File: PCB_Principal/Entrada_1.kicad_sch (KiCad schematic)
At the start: 17 parts, among them U21 TL071

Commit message: Iniciando PCB...
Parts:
- U101: renamed from U21; footprint Package_DIP:CERDIP-8_W7.62mm_SideBrazed_LongPads_Socket -> Package_DIP:CERDIP-8_W7.62mm_SideBrazed_LongPads
- renumbered C21 to C101, C22 to C102, C23 to C103, C24 to C104, C25 to C105, D21 to D101, D22 to D102, R21 to R101, R22 to R102, R23 to R103, R24 to R104, R25 to R105, R26 to R106, R27 to R107, R28 to R108, RV21 to RV101
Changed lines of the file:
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@@
 		(on_board yes)
 		(dnp no)
-		(property "Reference" "R21"
+		(property "Reference" "R101"
 			(at 91.44 89.408 90)
 			(effects
@@
 			(project "ISPEL-CAD_v1"
 				(path "/f66f0001-c0b9-4d2c-a26f-f2bac9dfd594/c2e6e06f-39d1-4f26-9e70-a3bc9c97e1f0"
-					(reference "R21")
+					(reference "R101")
 					(unit 1)
 				)
@@
 		(on_board yes)
 		(dnp no)
-		(property "Reference" "RV21"
+		(property "Reference" "RV101"
 			(at 143.51 106.68 90)
 			(effects
@@
 			(project "ISPEL-CAD_v1"
 				(path "/f66f0001-c0b9-4d2c-a26f-f2bac9dfd594/c2e6e06f-39d1-4f26-9e70-a3bc9c97e1f0"
-					(reference "RV21")
+					(reference "RV101")
 					(unit 1)
 				)
@@
 		(dnp no)
 		(fields_autoplaced yes)
-		(property "Reference" "#PWR027"
+		(property "Reference" "#PWR0107"
 			(at 208.28 113.03 0)
 			(effects
@@
 			(project "ISPEL-CAD_v1"
 				(path "/f66f0001-c0b9-4d2c-a26f-f2bac9dfd594/c2e6e06f-39d1-4f26-9e70-a3bc9c97e1f0"
-					(reference "#PWR027")
+					(reference "#PWR0107")
 					(unit 1)
 				)
@@
 		(on_board yes)
 		(dnp no)
-		(property "Reference" "R28"
+		(property "Reference" "R108"
 			(at 209.55 100.33 0)
 			(effects
@@
 			(project "ISPEL-CAD_v1"
 				(path "/f66f0001-c0b9-4d2c-a26f-f2bac9dfd594/c2e6e06f-39d1-4f26-9e70-a3bc9c97e1f0"
-					(reference "R28")
+					(reference "R108")
 					(unit 1)
 				)
@@
 		(dnp no)
 		(fields_autoplaced yes)
-		(property "Reference" "D22"
+		(property "Reference" "D102"
 			(at 100.33 109.2199 90)
 			(effects
@@
 			(project "ISPEL-CAD_v1"
 				(path "/f66f0001-c0b9-4d2c-a26f-f2bac9dfd594/c2e6e06f-39d1-4f26-9e70-a3bc9c97e1f0"
-					(reference "D22")
+					(reference "D102")
 					(unit 1)
 				)
@@
 		(dnp no)
 		(fields_autoplaced yes)
-		(property "Reference" "D21"
+		(property "Reference" "D101"
 			(at 100.33 71.1199 90)
 			(effects
@@
 			(project ""
 				(path "/f66f0001-c0b9-4d2c-a26f-f2bac9dfd594/c2e6e06f-39d1-4f26-9e70-a3bc9c97e1f0"
-					(reference "D21")
+					(reference "D101")
 					(unit 1)
 				)
@@
 		(dnp no)
 		(fields_autoplaced yes)
-		(property "Reference" "C25"
+		(property "Reference" "C105"
 			(at 217.17 73.66 90)
 			(effects
@@
 			(project "ISPEL-CAD_v1"
 				(path "/f66f0001-c0b9-4d2c-a26f-f2bac9dfd594/c2e6e06f-39d1-4f26-9e70-a3bc9c97e1f0"
-					(reference "C25")
+					(reference "C105")
 					(unit 1)
 				)
@@
 		(on_board yes)
 		(dnp no)
-		(property "Reference" "C24"
+		(property "Reference" "C104"
 			(at 146.05 125.222 90)
 			(effects
@@
 			(project "ISPEL-CAD_v1"
 				(path "/f66f0001-c0b9-4d2c-a26f-f2bac9dfd594/c2e6e06f-39d1-4f26-9e70-a3bc9c97e1f0"
-					(reference "C24")
+					(reference "C104")
 					(unit 1)
 				)
@@
 		(on_board yes)
 		(dnp no)
-		(property "Reference" "R25"
+		(property "Reference" "R105"
 			(at 195.58 86.36 0)
 			(effects
@@
 			(project "ISPEL-CAD_v1"
 				(path "/f66f0001-c0b9-4d2c-a26f-f2bac9dfd594/c2e6e06f-39d1-4f26-9e70-a3bc9c97e1f0"
-					(reference "R25")
+					(reference "R105")
 					(unit 1)
 				)
@@
 		(on_board yes)
 		(dnp no)
-		(property "Reference" "R22"
+		(property "Reference" "R102"
 			(at 104.14 89.408 90)
 			(effects
@@
 			(project "ISPEL-CAD_v1"
 				(path "/f66f0001-c0b9-4d2c-a26f-f2bac9dfd594/c2e6e06f-39d1-4f26-9e70-a3bc9c97e1f0"
-					(reference "R22")
+					(reference "R102")
 					(unit 1)
 				)
@@
 		(dnp no)
 		(fields_autoplaced yes)
-		(property "Reference" "#PWR026"
+		(property "Reference" "#PWR0105"
 			(at 152.4 127 0)
 			(effects
@@
 			(project "ISPEL-CAD_v1"
 				(path "/f66f0001-c0b9-4d2c-a26f-f2bac9dfd594/c2e6e06f-39d1-4f26-9e70-a3bc9c97e1f0"
-					(reference "#PWR026")
+					(reference "#PWR0105")
 					(unit 1)
 				)
@@
 		(dnp no)
 		(fields_autoplaced yes)
-		(property "Reference" "#PWR028"
+		(property "Reference" "#PWR0108"
 			(at 222.25 90.17 0)
 			(effects
@@
 			(project "ISPEL-CAD_v1"
 				(path "/f66f0001-c0b9-4d2c-a26f-f2bac9dfd594/c2e6e06f-39d1-4f26-9e70-a3bc9c97e1f0"
-					(reference "#PWR028")
+					(reference "#PWR0108")
 					(unit 1)
 				)
@@
 		(dnp no)
 		(fields_autoplaced yes)
-		(property "Reference" "#PWR025"
+		(property "Reference" "#PWR0104"
 			(at 152.4 76.2 0)
 			(effects
@@
 			(project "ISPEL-CAD_v1"
 				(path "/f66f0001-c0b9-4d2c-a26f-f2bac9dfd594/c2e6e06f-39d1-4f26-9e70-a3bc9c97e1f0"
-					(reference "#PWR025")
+					(reference "#PWR0104")
 					(unit 1)
 				)
@@
 		(dnp no)
 		(fields_autoplaced yes)
-		(property "Reference" "C21"
+		(property "Reference" "C101"
 			(at 87.63 96.5262 0)
 			(effects
@@
 			(project "ISPEL-CAD_v1"
 				(path "/f66f0001-c0b9-4d2c-a26f-f2bac9dfd594/c2e6e06f-39d1-4f26-9e70-a3bc9c97e1f0"
-					(reference "C21")
+					(reference "C101")
 					(unit 1)
 				)
@@
 		(on_board yes)
 		(dnp no)
-		(property "Reference" "R24"
+		(property "Reference" "R104"
 			(at 185.42 91.948 90)
 			(effects
@@
 			(project "ISPEL-CAD_v1"
 				(path "/f66f0001-c0b9-4d2c-a26f-f2bac9dfd594/c2e6e06f-39d1-4f26-9e70-a3bc9c97e1f0"
-					(reference "R24")
+					(reference "R104")
 					(unit 1)
 				)
@@
 		(on_board yes)
 		(dnp no)
-		(property "Reference" "U21"
+		(property "Reference" "U101"
 			(at 142.24 86.36 0)
 			(effects
@@
 			)
 		)
-		(property "Footprint" "Package_DIP:CERDIP-8_W7.62mm_SideBrazed_LongPads_Socket"
+		(property "Footprint" "Package_DIP:CERDIP-8_W7.62mm_SideBrazed_LongPads"
 			(at 140.97 92.71 0)
 			(effects
@@
 			(project "ISPEL-CAD_v1"
 				(path "/f66f0001-c0b9-4d2c-a26f-f2bac9dfd594/c2e6e06f-39d1-4f26-9e70-a3bc9c97e1f0"
-					(reference "U21")
+					(reference "U101")
 					(unit 1)
 				)
@@
 		(on_board yes)
 		(dnp no)
-		(property "Reference" "R27"
+		(property "Reference" "R107"
 			(at 209.55 86.36 0)
 			(effects
@@
 			(project "ISPEL-CAD_v1"
 				(path "/f66f0001-c0b9-4d2c-a26f-f2bac9dfd594/c2e6e06f-39d1-4f26-9e70-a3bc9c97e1f0"
-					(reference "R27")
+					(reference "R107")
 					(unit 1)
 				)
@@
 		(dnp no)
 		(fields_autoplaced yes)
-		(property "Reference" "#PWR023"
+		(property "Reference" "#PWR0102"
 			(at 110.49 110.49 0)
 			(effects
@@
 			(project "ISPEL-CAD_v1"
 				(path "/f66f0001-c0b9-4d2c-a26f-f2bac9dfd594/c2e6e06f-39d1-4f26-9e70-a3bc9c97e1f0"
-					(reference "#PWR023")
+					(reference "#PWR0102")
 					(unit 1)
 				)
@@
 		(dnp no)
 		(fields_autoplaced yes)
-		(property "Reference" "#PWR022"
+		(property "Reference" "#PWR0101"
 			(at 85.09 110.49 0)
 			(effects
@@
 			(project "ISPEL-CAD_v1"
 				(path "/f66f0001-c0b9-4d2c-a26f-f2bac9dfd594/c2e6e06f-39d1-4f26-9e70-a3bc9c97e1f0"
-					(reference "#PWR022")
+					(reference "#PWR0101")
 					(unit 1)
 				)
@@
 		(on_board yes)
 		(dnp no)
-		(property "Reference" "R23"
+		(property "Reference" "R103"
 			(at 111.76 99.06 0)
 			(effects
@@
 			(project "ISPEL-CAD_v1"
 				(path "/f66f0001-c0b9-4d2c-a26f-f2bac9dfd594/c2e6e06f-39d1-4f26-9e70-a3bc9c97e1f0"
-					(reference "R23")
+					(reference "R103")
 					(unit 1)
 				)
@@
 		(on_board yes)
 		(dnp no)
-		(property "Reference" "R26"
+		(property "Reference" "R106"
 			(at 201.93 91.948 90)
 			(effects
@@
 			(project "ISPEL-CAD_v1"
 				(path "/f66f0001-c0b9-4d2c-a26f-f2bac9dfd594/c2e6e06f-39d1-4f26-9e70-a3bc9c97e1f0"
-					(reference "R26")
+					(reference "R106")
 					(unit 1)
 				)
@@
 		(dnp no)
 		(fields_autoplaced yes)
-		(property "Reference" "#PWR024"
+		(property "Reference" "#PWR0103"
 			(at 143.51 119.38 0)
 			(effects
@@
 			(project "ISPEL-CAD_v1"
 				(path "/f66f0001-c0b9-4d2c-a26f-f2bac9dfd594/c2e6e06f-39d1-4f26-9e70-a3bc9c97e1f0"
-					(reference "#PWR024")
+					(reference "#PWR0103")
 					(unit 1)
 				)
@@
 		(dnp no)
 		(fields_autoplaced yes)
-		(property "Reference" "C23"
+		(property "Reference" "C103"
 			(at 146.05 60.96 90)
 			(effects
@@
 			(project "ISPEL-CAD_v1"
 				(path "/f66f0001-c0b9-4d2c-a26f-f2bac9dfd594/c2e6e06f-39d1-4f26-9e70-a3bc9c97e1f0"
-					(reference "C23")
+					(reference "C103")
 					(unit 1)
 				)
@@
 		(dnp no)
 		(fields_autoplaced yes)
-		(property "Reference" "C22"
+		(property "Reference" "C102"
 			(at 91.4463 78.74 90)
 			(effects
@@
 			(project "ISPEL-CAD_v1"
 				(path "/f66f0001-c0b9-4d2c-a26f-f2bac9dfd594/c2e6e06f-39d1-4f26-9e70-a3bc9c97e1f0"
-					(reference "C22")
-					(unit 1)
-				)
+					(reference "C102")
+					(unit 1)
+				)

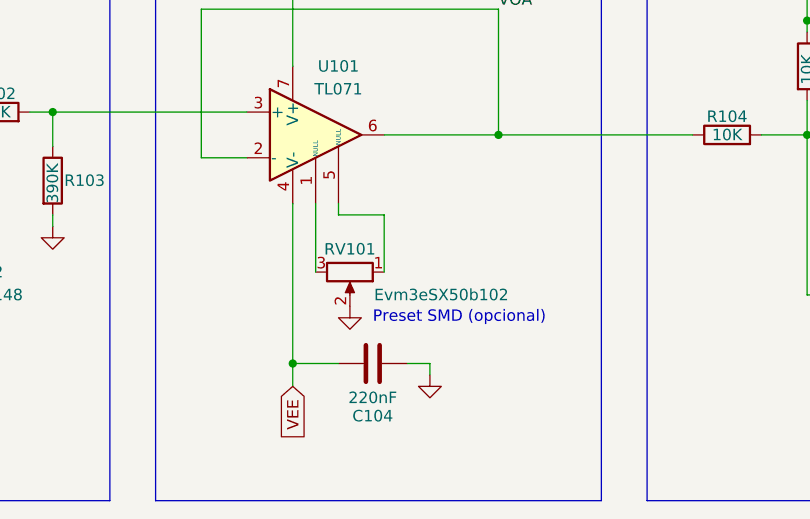
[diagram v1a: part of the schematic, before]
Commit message: Placa con conector J8.
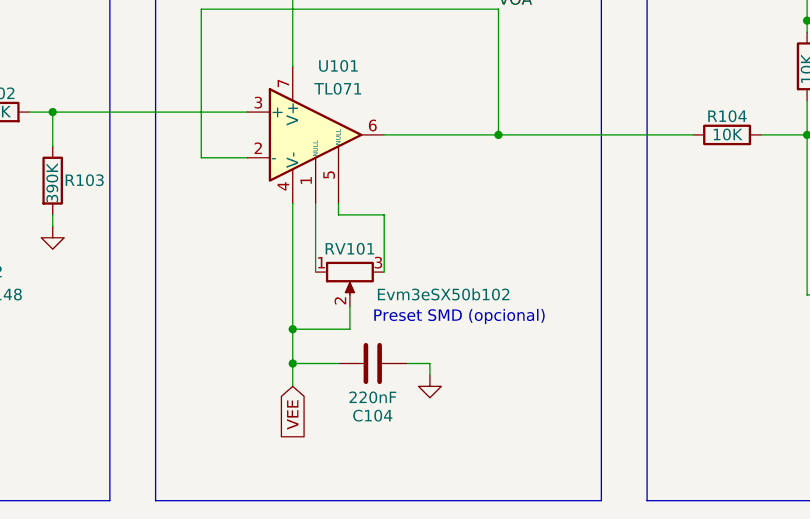
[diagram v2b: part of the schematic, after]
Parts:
- U101: footprint Package_DIP:CERDIP-8_W7.62mm_SideBrazed_LongPads -> Package_DIP:CERDIP-8_W7.62mm_SideBrazed_LongPads_Socket
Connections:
- net GND: no longer RV101.2
- net VEE: now also RV101.2
- net at RV101.1: now also U101.1 (NULL); no longer U101.5 (NULL)
- net at RV101.3: now also U101.5 (NULL); no longer U101.1 (NULL)
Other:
- moved on the sheet: RV101
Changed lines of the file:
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@@
+	)
+	(junction
+		(at 137.16 115.57)
+		(diameter 0)
+		(color 0 0 0 0)
 	)
 	(junction
@@
 	(wire
 		(pts
-			(xy 137.16 101.6) (xy 137.16 119.38)
+			(xy 137.16 115.57) (xy 137.16 119.38)
+		)
+		(stroke
+			(width 0)
+			(type default)
+		)
+	)
+	(wire
+		(pts
+			(xy 137.16 101.6) (xy 137.16 115.57)
 		)
 		(stroke
@@
 	(wire
 		(pts
+			(xy 137.16 115.57) (xy 143.51 115.57)
+		)
+		(stroke
+			(width 0)
+			(type default)
+		)
+	)
+	(wire
+		(pts
 			(xy 208.28 93.98) (xy 208.28 96.52)
 		)
@@
 		(pts
 			(xy 127 80.01) (xy 160.02 80.01)
+		)
+		(stroke
+			(width 0)
+			(type default)
+		)
+	)
+	(wire
+		(pts
+			(xy 143.51 113.03) (xy 143.51 115.57)
 		)
 		(stroke
@@
 	(symbol
 		(lib_id "Device:R_Potentiometer")
-		(at 143.51 109.22 270)
+		(at 143.51 109.22 90)
+		(mirror x)
 		(unit 1)
 		(exclude_from_sim no)
@@
 		)
 		(property "Value" "Evm3eSX50b102"
-			(at 153.67 111.76 90)
+			(at 153.924 111.76 90)
 			(effects
 				(font
@@
 			)
 		)
-		(property "Footprint" "Package_DIP:CERDIP-8_W7.62mm_SideBrazed_LongPads"
+		(property "Footprint" "Package_DIP:CERDIP-8_W7.62mm_SideBrazed_LongPads_Socket"
 			(at 140.97 92.71 0)
 			(effects
@@
 					(unit 1)
 				)
-			)
-		)
-	)
-	(symbol
-		(lib_id "power:GND")
-		(at 143.51 113.03 0)
-		(unit 1)
-		(exclude_from_sim no)
-		(in_bom yes)
-		(on_board yes)
-		(dnp no)
-		(fields_autoplaced yes)
-		(property "Reference" "#PWR0103"
-			(at 143.51 119.38 0)
-			(effects
-				(font
-					(size 1.27 1.27)
-				)
-				(hide yes)
-			)
-		)
-		(property "Value" "GND"
-			(at 143.51 118.11 0)
-			(effects
-				(font
-					(size 1.27 1.27)
-				)
-				(hide yes)
-			)
-		)
-		(property "Footprint" ""
-			(at 143.51 113.03 0)
-			(effects
-				(font
-					(size 1.27 1.27)
-				)
-				(hide yes)
-			)
-		)
-		(property "Datasheet" ""
-			(at 143.51 113.03 0)
-			(effects
-				(font
-					(size 1.27 1.27)
-				)
-				(hide yes)
-			)
-		)
-		(property "Description" "Power symbol creates a global label with name \"GND\" , ground"
-			(at 143.51 113.03 0)
-			(effects
-				(font
-					(size 1.27 1.27)
-				)
-				(hide yes)
-			)
-		)
-		(pin "1"
-		)
-		(instances
-			(project "ISPEL-CAD_v1"
-				(path "/f66f0001-c0b9-4d2c-a26f-f2bac9dfd594/c2e6e06f-39d1-4f26-9e70-a3bc9c97e1f0"
-					(reference "#PWR0103")
-					(unit 1)
-				)

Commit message: Revisión 1. Con prototipo ISPEL Beta 2024 en fase de prueba.
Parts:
- C102: value 3.3pF -> 5pF
- U101: value TL071 -> CA3140
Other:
- title: Entrada 1 (ISPEL Beta 2024) -> Entrada 1 (ISPEL Beta)
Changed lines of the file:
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@@
 	(paper "A4")
 	(title_block
-		(title "Entrada 1 (ISPEL Beta 2024)")
-		(rev "2 (GC)")
+		(title "Entrada 1 (ISPEL Beta)")
+		(date "2025-04-04")
+		(rev "1")
 		(company "UNDAV")
 	)
@@
 			)
 		)
-		(property "Value" "TL071"
+		(property "Value" "CA3140"
 			(at 142.24 88.9 0)
 			(effects
@@
 			)
 		)
-		(property "Datasheet" "http://www.ti.com/lit/ds/symlink/tl071.pdf"
+		(property "Datasheet" "https://www.renesas.com/en/document/dst/ca3140-ca3140a-datasheet?r=505296"
 			(at 143.51 90.17 0)
 			(effects
@@
 			)
 		)
-		(property "Description" "Single Low-Noise JFET-Input Operational Amplifiers, DIP-8/SOIC-8"
+		(property "Description" "4.5MHz, BiMOS Operational Amplifier with MOSFET Input/Bipolar Output"
 			(at 139.7 93.98 0)
 			(effects
@@
 			)
 		)
-		(property "Value" "3.3pF"
+		(property "Value" "5pF"
 			(at 91.4463 81.28 90)
 			(effects
